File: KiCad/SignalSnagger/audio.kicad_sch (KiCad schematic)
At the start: 59 parts, among them J301 35RASMT2BHSNTRX, J302 36-5005-ND, J304 36-5006-ND, J903 36-5005-ND, U302 TS912IDT, U304 LM386, U901 TS912IDT, U902 LM386

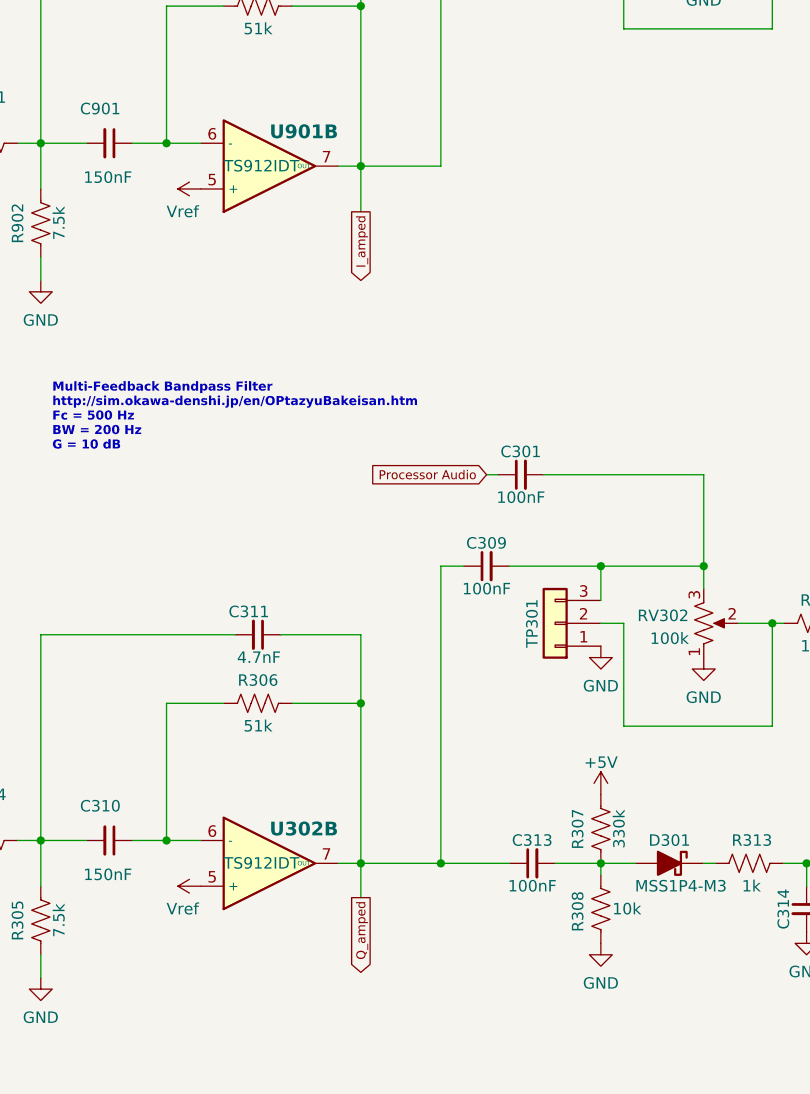
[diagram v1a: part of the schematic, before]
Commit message: Rev 0.321
o Added voltage divider for the I_AMPED and Q_AMPED ADC inputs to the processor.
o Generated new Gerbers
o Generated new BOM files
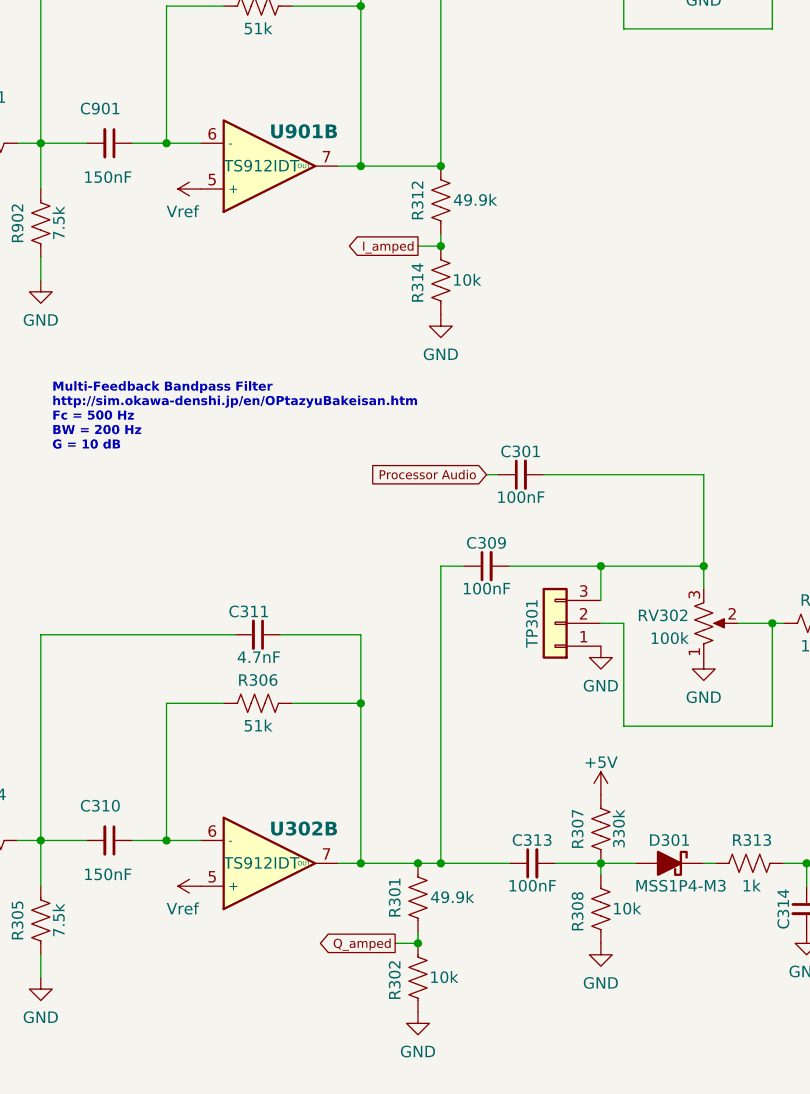
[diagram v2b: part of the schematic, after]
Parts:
- added R301, R312: 49.9k, Resistor_SMD:R_0603_1608Metric, symbol Device:R_US
- added R302, R314: 10k, Resistor_SMD:R_0603_1608Metric, symbol Device:R_US
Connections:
- net GND: now also R302.2, R314.2
- net I_amped: now also R312.2, R314.1; no longer C902.1, C903.1, R903.2, U901.7 (OUT)
- net Q_amped: now also R301.2, R302.1; no longer C309.1, C311.1, C313.1, R306.2, U302.7 (OUT)
- new net: C309.1, C311.1, C313.1, R301.1, R306.2, U302.7 (OUT)
- new net: C902.1, C903.1, R312.1, R903.2, U901.7 (OUT)

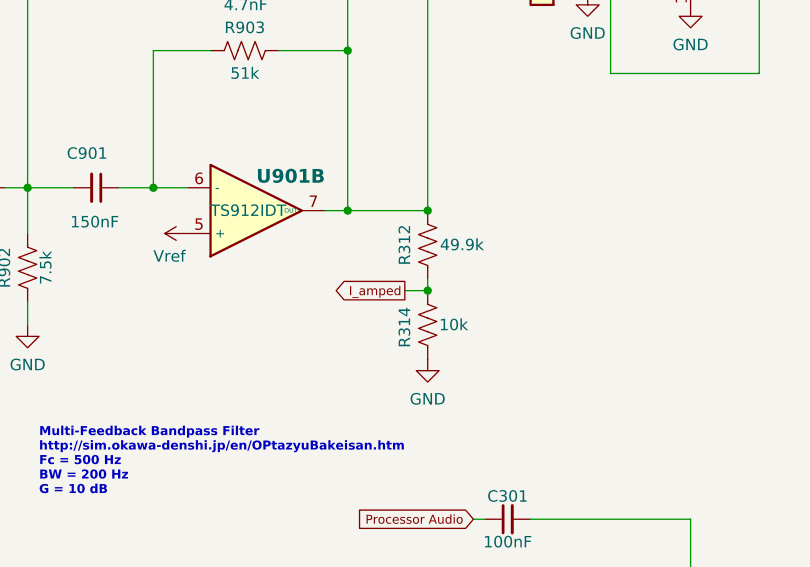
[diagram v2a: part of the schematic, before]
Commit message: Added voltage divider
o Added voltage dividers for I_AMPED and Q_AMPED
o Regenerated Gerbers
o Updated schematic
o Updated BOM files
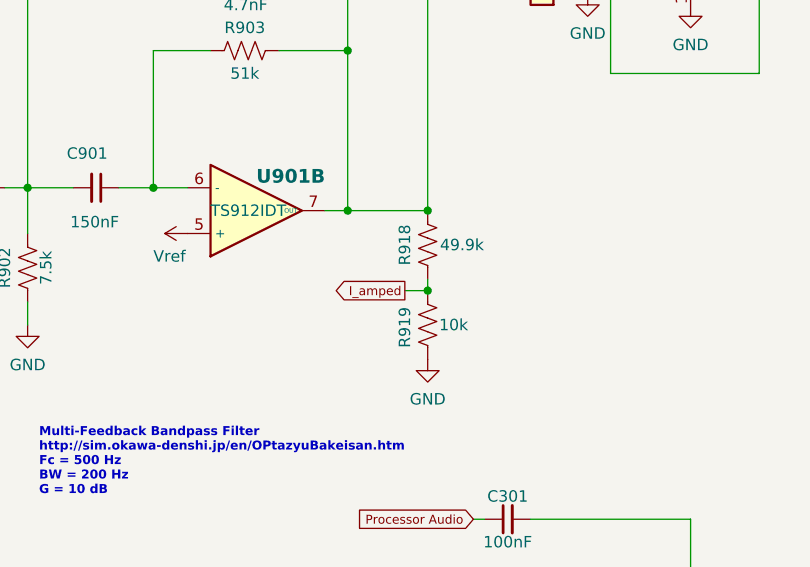
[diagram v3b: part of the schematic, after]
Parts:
- renumbered R312 to R918, R314 to R919
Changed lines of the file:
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@@
   (symbol (lib_id "Device:R_US") (at 106.68 77.47 0) (unit 1)
     (in_bom yes) (on_board yes)
-    (property "Reference" "R312" (id 0) (at 104.14 77.47 90))
+    (property "Reference" "R918" (id 0) (at 104.14 77.47 90))
     (property "Value" "49.9k" (id 1) (at 110.49 77.47 0))
     (property "Footprint" "Resistor_SMD:R_0603_1608Metric" (id 2) (at 107.696 77.724 90)
@@
   (symbol (lib_id "Device:R_US") (at 106.68 86.36 0) (unit 1)
     (in_bom yes) (on_board yes)
-    (property "Reference" "R314" (id 0) (at 104.14 88.9 90)
-      (effects (font (size 1.27 1.27)) (justify left))
-    )
+    (property "Reference" "R919" (id 0) (at 104.14 88.9 90)
+      (effects (font (size 1.27 1.27)) (justify left))
+    )

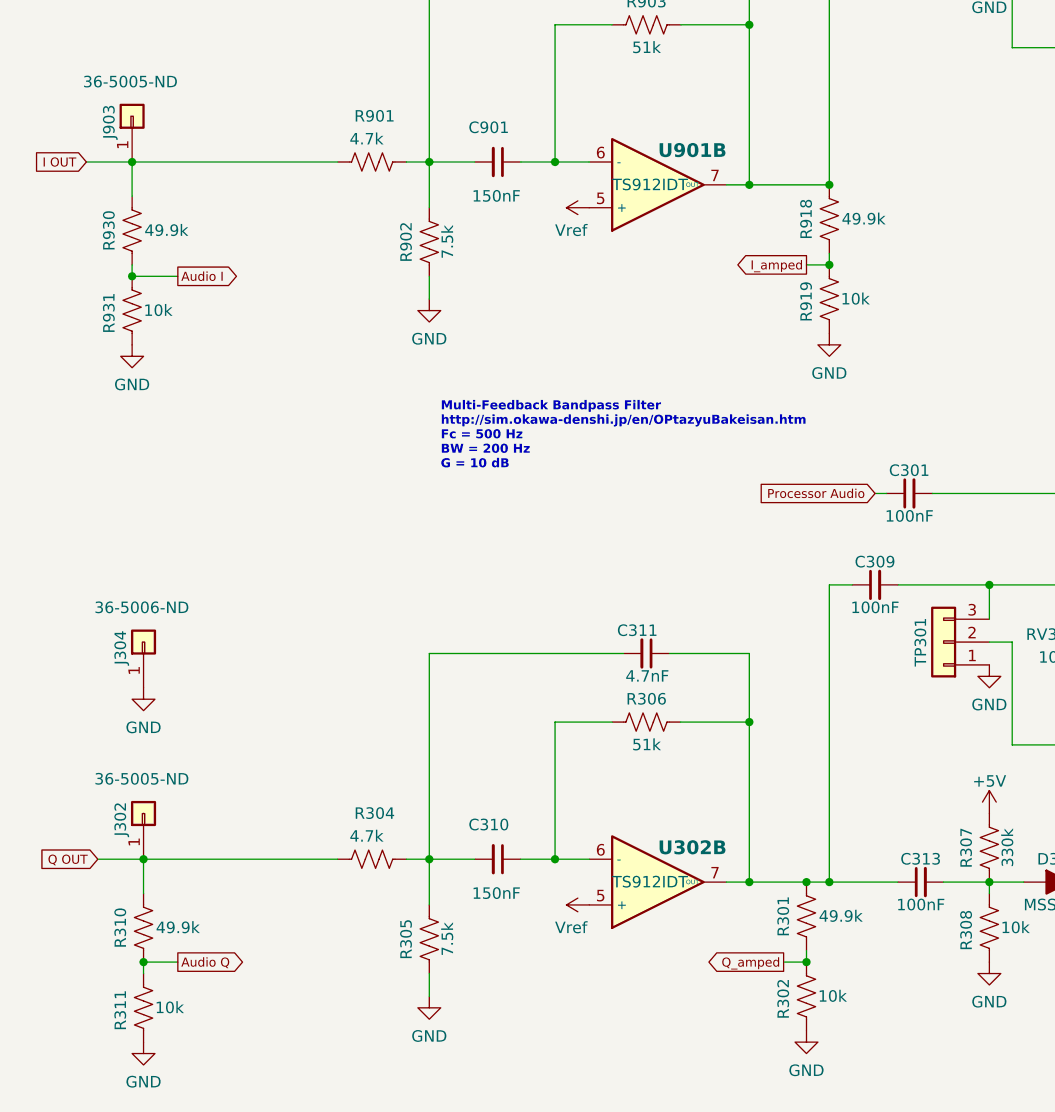
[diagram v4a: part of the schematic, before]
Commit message: Schematic Ver 0.323
o Updated schematic with changes to audio sampling interface locations
o PCB and Gerbers still need to be updated to be in sync with this schematic
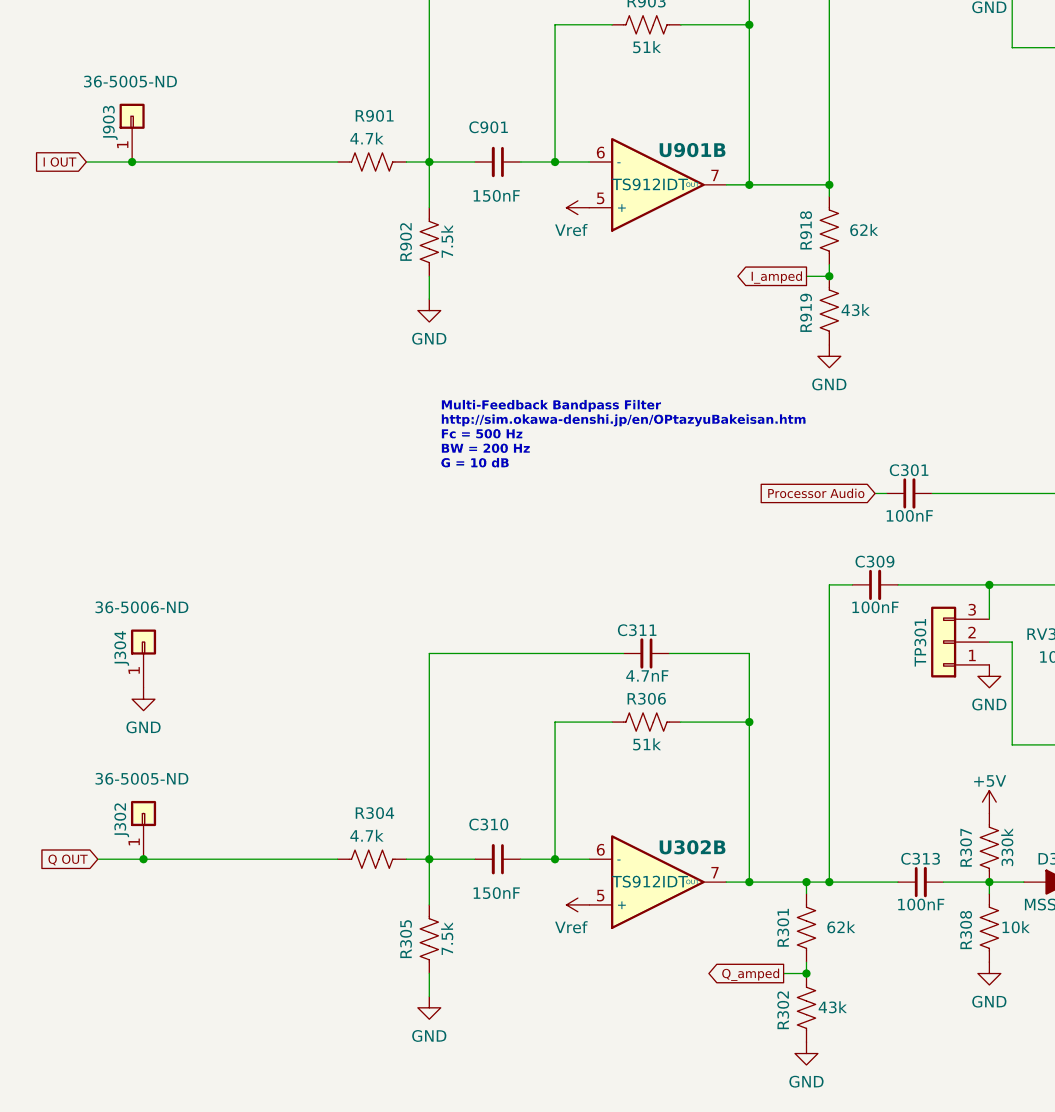
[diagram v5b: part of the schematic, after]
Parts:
- removed R310, R930: 49.9k, Resistor_SMD:R_0603_1608Metric, symbol Device:R_US
- removed R311, R931: 10k, Resistor_SMD:R_0603_1608Metric, symbol Device:R_US
- R301, R918: value 49.9k -> 62k; Digi-Key Part No. 311-49.9KLDCT-ND -> YAG2754CT-ND; Link https://www.digikey.com/en/products/detail/yageo/AC0603FR-0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 -> https://www.digikey.com/en/products/detail/yageo/RC0201FR-0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; Manufacturer PN AC0603FR-0749K9L -> RC0201FR-0762KL
- R302, R919: value 10k -> 43k; Digi-Key Part No. 311-10.0KHRCT-ND -> 311-43KGRCT-ND; Link https://www.digikey.com/en/products/detail/yageo/RC0603FR-0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 -> https://www.digikey.com/en/products/detail/yageo/RC0603JR-0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; Manufacturer PN RC0603FR-0710KL -> RC0603JR-0743KL
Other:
- moved on the sheet: R918, R919

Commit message: Schematic Updates
Schematic version 0.323.
Schematic and BOM updates only.
For next rev PCB.
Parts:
- removed RV302, RV901: 100k, Potentiometer_SMD:Potentiometer_Bourns_TC33X_Vertical, symbol Device:R_Potentiometer_US
- added C303, C913: 100nF, Capacitor_SMD:C_0603_1608Metric, symbol Device:C_Small
- added R312: 4.7k, Resistor_SMD:R_0603_1608Metric, symbol Device:R_US
- added R314: 100, Resistor_SMD:R_0603_1608Metric, symbol Device:R_US
- added U303, U903: MCP4018T-503E, Package_TO_SOT_SMD:SOT-363_SC-70-6B, symbol Potentiometer_Digital:MCP4018-xxxxLT
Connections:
- net +5V: now also C303.2, C913.2, U303.1 (VDD), U903.1 (VDD)
- net GND: now also C303.1, C913.1, U303.2 (VSS), U903.2 (VSS)
- net at R907.1, TP901.2 (Pin_2): now also U903.5 (W)
- net at C903.2, TP901.3 (Pin_3): now also U903.6 (A)
- net at R303.1, TP301.2 (Pin_2): now also U303.5 (W)
- new net: R312.2, R314.1, TP301.3 (Pin_3), U303.6 (A)
- new net: C309.2, R314.2
- new net: C301.2, R312.1
- new net SCL0: U303.3 (SCL)
- new net SCL1: U903.3 (SCL)
- new net SDA0: U303.4 (SDA)
- new net SDA1: U903.4 (SDA)
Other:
- note added: "Pot slave Addr: 0x2F"
- moved on the sheet: C301, C309, C310, C311, C312, C313, C314, C319, C320, C321, C322, C324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
